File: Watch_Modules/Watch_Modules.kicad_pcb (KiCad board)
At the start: 2 copper layers, 15.2 x 25 mm, 1 part, among them J1 Conn_01x06_Female

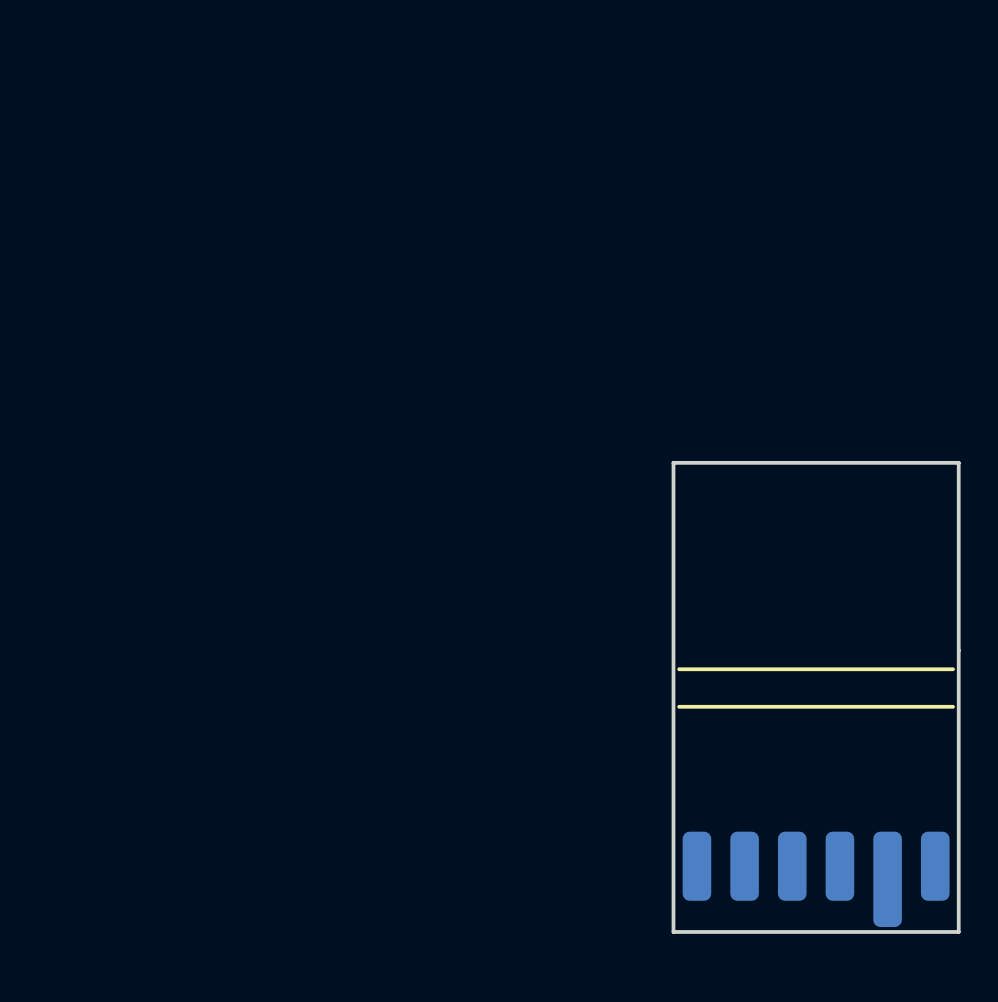
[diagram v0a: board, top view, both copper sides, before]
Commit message: Graphical fixes, minor electrical fixes and enviro sensor module trial
Fixed some component values and added i2c pullups
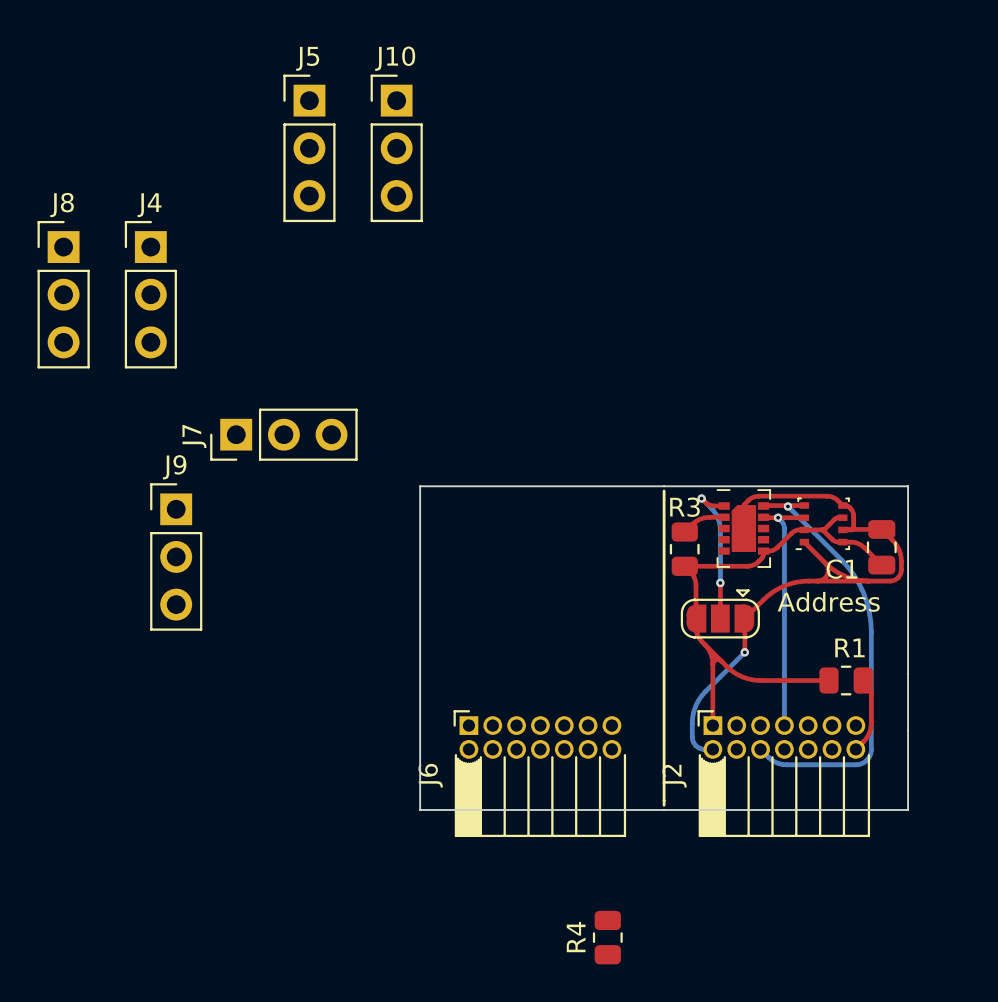
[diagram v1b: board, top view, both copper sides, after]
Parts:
- removed J1: Conn_01x06_Female, 70AAJ-6-M0G:ModuleConnector
- added Address: SolderJumper_3_Open, Jumper:SolderJumper-3_P1.3mm_Open_RoundedPad1.0x1.5mm, F.Cu at (130.5, 92.3)
- added C1: 100nF, Capacitor_SMD:C_0805_2012Metric, F.Cu at (139.1, 88.5)
- added J10: D39, Connector_PinHeader_2.54mm:PinHeader_1x03_P2.54mm_Vertical, F.Cu at (113.2, 64.7)
- added J2: Conn_02x07_Counter_Clockwise, Connector_PinSocket_1.27mm:PinSocket_2x07_P1.27mm_Horizontal, F.Cu at (130.1, 98.0)
- added J4: D12/A, Connector_PinHeader_2.54mm:PinHeader_1x03_P2.54mm_Vertical, F.Cu at (100.2, 72.5)
- added J5: D18/A, Connector_PinHeader_2.54mm:PinHeader_1x03_P2.54mm_Vertical, F.Cu at (108.6, 64.7)
- added J6: Conn_02x07_Counter_Clockwise, Connector_PinSocket_1.27mm:PinSocket_2x07_P1.27mm_Horizontal, F.Cu at (117.1, 98.0)
- added J7: D11/A, Connector_PinHeader_2.54mm:PinHeader_1x03_P2.54mm_Vertical, F.Cu at (104.7, 82.5)
- added J8: D42, Connector_PinHeader_2.54mm:PinHeader_1x03_P2.54mm_Vertical, F.Cu at (95.5, 72.5)
- added J9: D10/A, Connector_PinHeader_2.54mm:PinHeader_1x03_P2.54mm_Vertical, F.Cu at (101.5, 86.5)
- added R1: NC, Resistor_SMD:R_0805_2012Metric, F.Cu at (137.2, 95.6)
- added R3: 4.7K, Resistor_SMD:R_0805_2012Metric, F.Cu at (128.6, 88.6)
- added R4: NC, Resistor_SMD:R_0805_2012Metric, F.Cu at (124.5, 109.3)
- added U1: BME280, Package_LGA:Bosch_LGA-8_2.5x2.5mm_P0.65mm_ClockwisePinNumbering, F.Cu at (136.0, 87.2)
- added U2: CCS811, Package_LGA:AMS_LGA-10-1EP_2.7x4mm_P0.6mm, F.Cu at (131.8, 87.5)
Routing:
- net Net-(Address_selector1-Pad1): track 0.00 -> 36.0 mm, vias 0 -> 1
- net Net-(Address_selector1-Pad3): track 0.00 -> 30.3 mm
- net Net-(J2-Pad6): track 0.00 -> 23.3 mm, vias 0 -> 1
- net Net-(J2-Pad7): track 0.00 -> 13.4 mm, vias 0 -> 1
- net Net-(Address_selector1-Pad2): track 0.00 -> 8.07 mm, vias 0 -> 2
- net Net-(J2-Pad14): track 0.00 -> 4.09 mm
- net Net-(R3-Pad2): track 0.00 -> 2.36 mm
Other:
- board size 15.2 x 25 mm -> 26 x 17.2 mm

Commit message: Fixed more connector problems
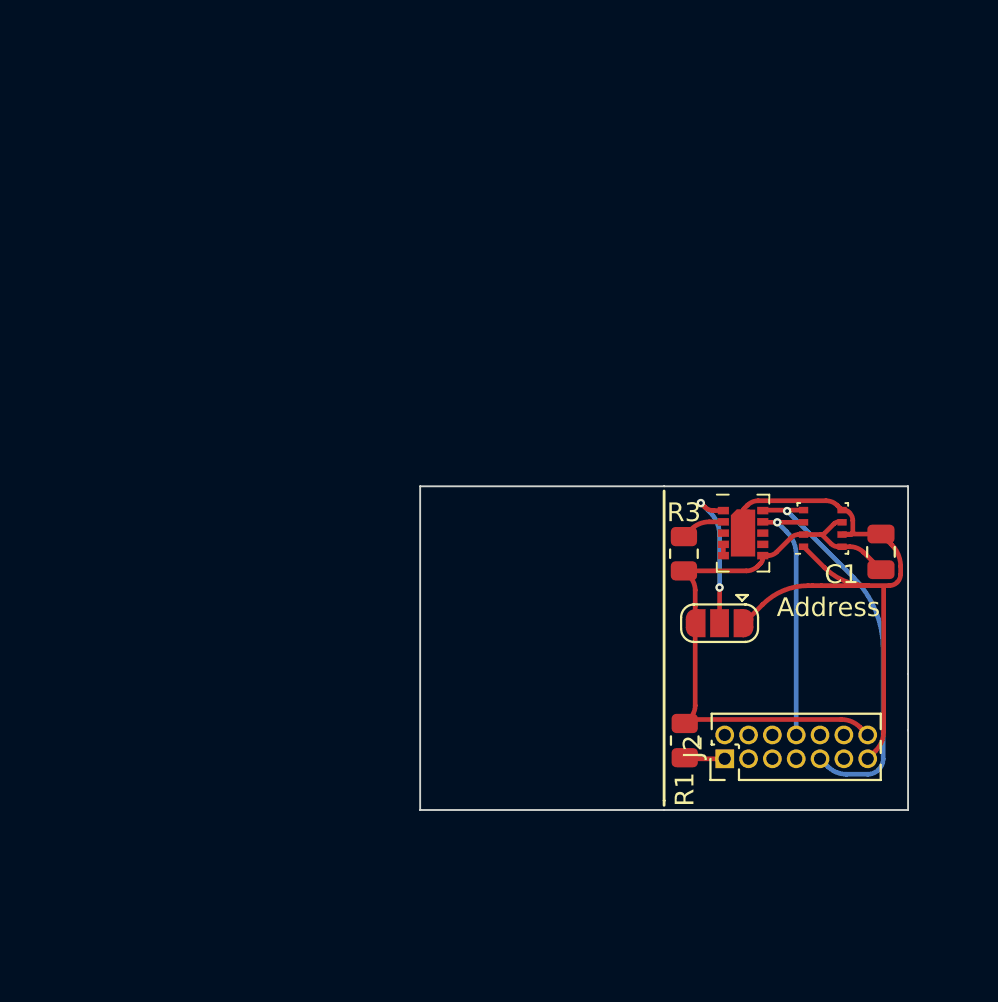
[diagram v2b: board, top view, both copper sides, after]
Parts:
- removed J10: D39, Connector_PinHeader_2.54mm:PinHeader_1x03_P2.54mm_Vertical
- removed J4: D12/A, Connector_PinHeader_2.54mm:PinHeader_1x03_P2.54mm_Vertical
- removed J5: D18/A, Connector_PinHeader_2.54mm:PinHeader_1x03_P2.54mm_Vertical
- removed J6: Conn_02x07_Counter_Clockwise, Connector_PinSocket_1.27mm:PinSocket_2x07_P1.27mm_Horizontal
- removed J7: D11/A, Connector_PinHeader_2.54mm:PinHeader_1x03_P2.54mm_Vertical
- removed J8: D42, Connector_PinHeader_2.54mm:PinHeader_1x03_P2.54mm_Vertical
- removed J9: D10/A, Connector_PinHeader_2.54mm:PinHeader_1x03_P2.54mm_Vertical
- removed R4: NC, Resistor_SMD:R_0805_2012Metric
- J2: footprint Connector_PinSocket_1.27mm:PinSocket_2x07_P1.27mm_Horizontal -> Connector_PinHeader_1.27mm:PinHeader_2x07_P1.27mm_Vertical
- moved R1 9.18 mm to (128.6, 98.8), turned to 90 degrees
- moved J2 1.88 mm to (130.7, 99.8)
- moved Address 0.25 mm to (130.5, 92.5)
- moved R3 0.25 mm to (128.6, 88.8)
- moved C1 0.25 mm to (139.1, 88.7)
- moved U1 0.25 mm to (136.0, 87.5)
- moved U2 0.25 mm to (131.7, 87.7)
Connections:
- J2 pad 1: Net-(Address_selector1-Pad3) -> Net-(J2-Pad1)
- J2 pad 13: unconnected-(J2-Pad13) -> Net-(Address_selector1-Pad1)
- J2 pad 14: Net-(J2-Pad14) -> Net-(Address_selector1-Pad3)
- J2 pad 2: Net-(Address_selector1-Pad1) -> unconnected-(J2-Pad2)
- J2 pad 6: Net-(J2-Pad6) -> unconnected-(J2-Pad6)
- J2 pad 7: Net-(J2-Pad7) -> unconnected-(J2-Pad7)
- J2 pad 8: unconnected-(J2-Pad8) -> Net-(U1-Pad3)
- J2 pad 9: unconnected-(J2-Pad9) -> Net-(U1-Pad4)
- R1 pad 1: Net-(J2-Pad14) -> Net-(J2-Pad1)
- U1 pad 3: Net-(J2-Pad7) -> Net-(U1-Pad3)
- U1 pad 4: Net-(J2-Pad6) -> Net-(U1-Pad4)
- U2 pad 10: Net-(J2-Pad6) -> Net-(U1-Pad4)
- U2 pad 9: Net-(J2-Pad7) -> Net-(U1-Pad3)
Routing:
- net Net-(J2-Pad6): track 23.3 -> 0.00 mm, vias 1 -> 0
- net Net-(U1-Pad4): track 0.00 -> 21.3 mm, vias 0 -> 1
- net Net-(U1-Pad3): track 0.00 -> 13.8 mm, vias 0 -> 1
- net Net-(J2-Pad7): track 13.4 -> 0.00 mm, vias 1 -> 0
- net Net-(J2-Pad14): track 4.09 -> 0.00 mm
- net Net-(J2-Pad1): track 0.00 -> 2.15 mm
- net Net-(Address_selector1-Pad3): track 30.3 -> 32.0 mm
- net Net-(Address_selector1-Pad1): track 36.0 -> 35.4 mm, vias 1 -> 0
- net Net-(U2-Pad4): track 0.00 -> 0.60 mm
